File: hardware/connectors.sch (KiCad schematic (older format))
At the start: 16 parts

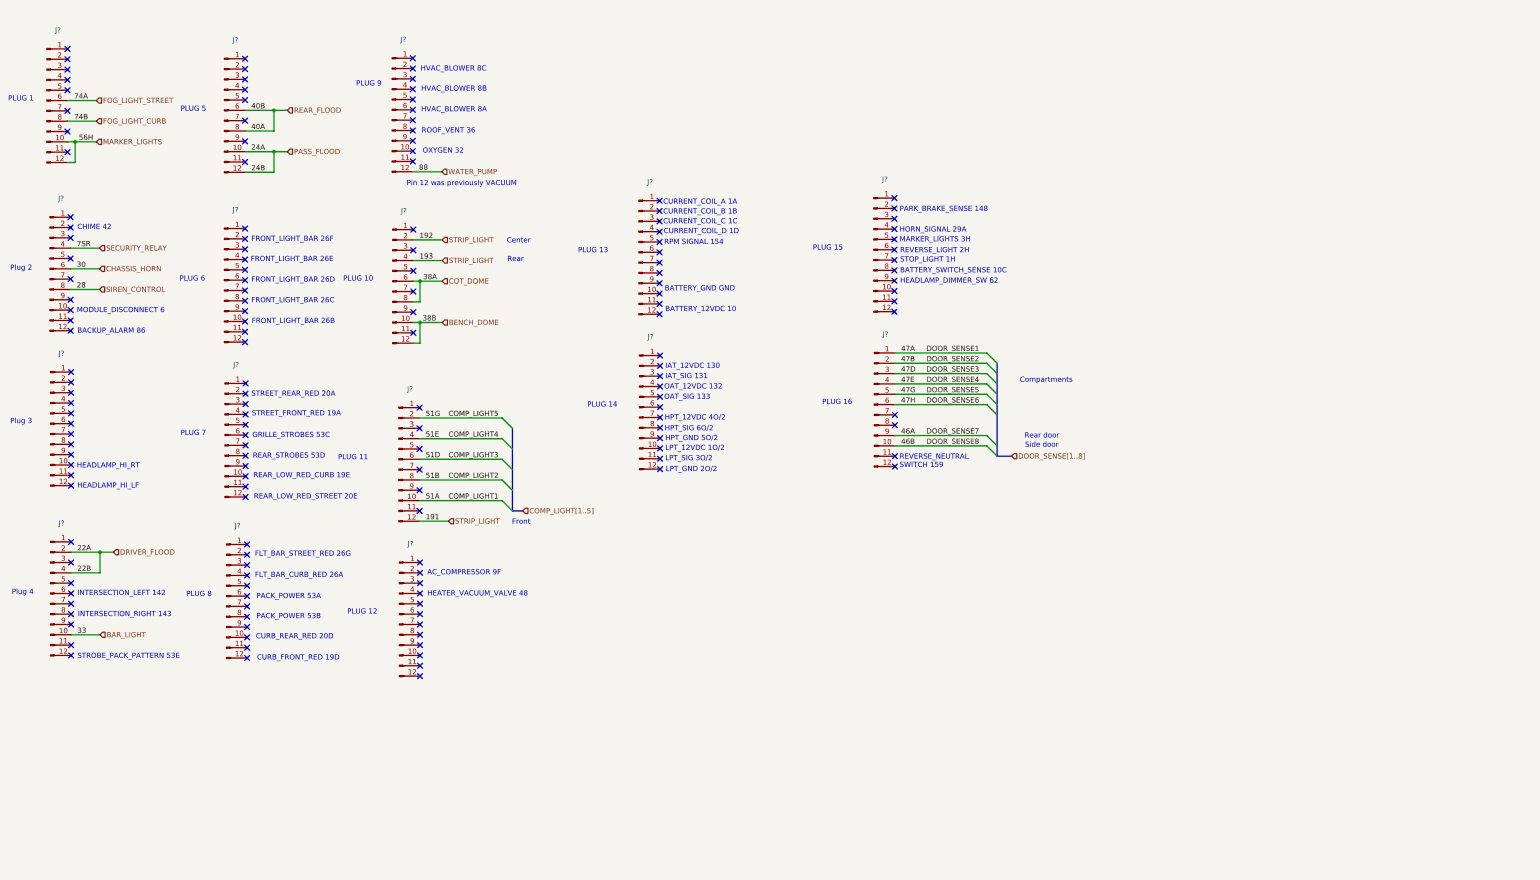
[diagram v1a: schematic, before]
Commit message: hardware: assign connectors corresponding references
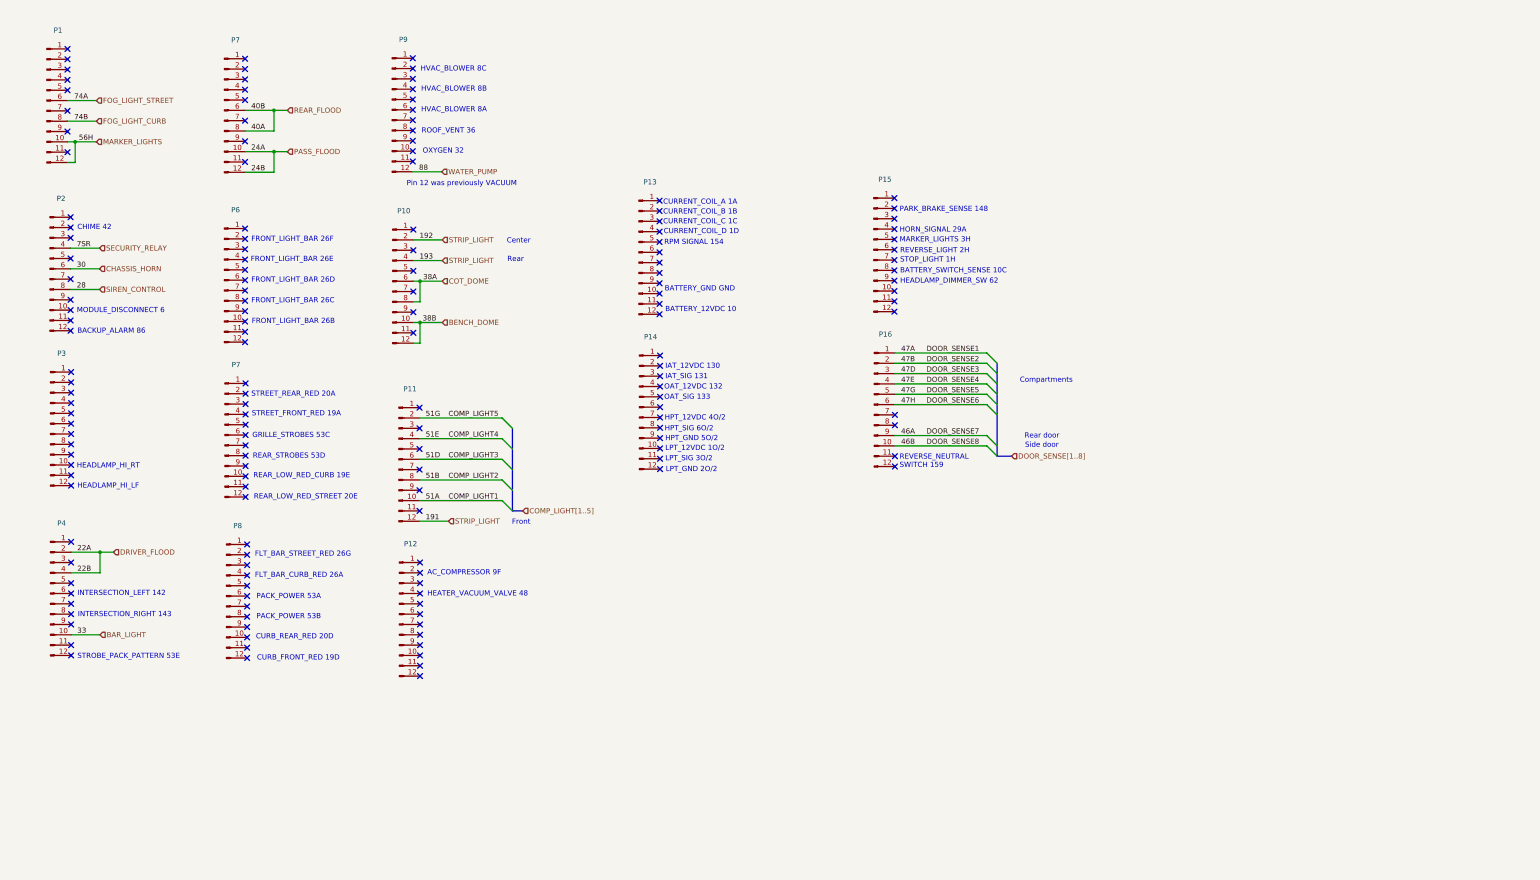
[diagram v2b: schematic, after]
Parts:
- gave numbers to parts that had none: 15
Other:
- note removed: "PLUG 1"
- note removed: "PLUG 10"
- note removed: "PLUG 11"
- note removed: "PLUG 12"
- note removed: "PLUG 13"
- note removed: "PLUG 14"
- note removed: "PLUG 15"
- note removed: "PLUG 16"
- note removed: "PLUG 5"
- note removed: "PLUG 6"
- note removed: "PLUG 7"
- note removed: "PLUG 8"
- note removed: "PLUG 9"
- note removed: "Plug 2"
- note removed: "Plug 3"
- note removed: "Plug 4"
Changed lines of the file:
@@
 P 1040 3290
 AR Path="/6060FD51" Ref="J?"  Part="1"
-AR Path="/605C149A/6060FD51" Ref="J?"  Part="1"
-F 0 "J?" H 1148 3971 50  0000 C CNN
+AR Path="/605C149A/6060FD51" Ref="P2"  Part="1"
+F 0 "P2" H 1148 3971 50  0000 C CNN
 F 1 "Conn_01x12_Male" H 1148 3880 50  0001 C CNN
 F 2 "Connector_Molex:Molex_KK-396_A-41791-0012_1x12_P3.96mm_Vertical" H 1040 3290 50  0001 C CNN
@@
 P 1045 4790
 AR Path="/60615EDC" Ref="J?"  Part="1"
-AR Path="/605C149A/60615EDC" Ref="J?"  Part="1"
-F 0 "J?" H 1153 5471 50  0000 C CNN
+AR Path="/605C149A/60615EDC" Ref="P3"  Part="1"
+F 0 "P3" H 1153 5471 50  0000 C CNN
 F 1 "Conn_01x12_Male" H 1153 5380 50  0001 C CNN
 F 2 "Connector_Molex:Molex_KK-396_A-41791-0012_1x12_P3.96mm_Vertical" H 1045 4790 50  0001 C CNN
@@
 P 1045 6435
 AR Path="/60615F08" Ref="J?"  Part="1"
-AR Path="/605C149A/60615F08" Ref="J?"  Part="1"
-F 0 "J?" H 1153 7116 50  0000 C CNN
+AR Path="/605C149A/60615F08" Ref="P4"  Part="1"
+F 0 "P4" H 1153 7116 50  0000 C CNN
 F 1 "Conn_01x12_Male" H 1153 7025 50  0001 C CNN
 F 2 "Connector_Molex:Molex_KK-396_A-41791-0012_1x12_P3.96mm_Vertical" H 1045 6435 50  0001 C CNN
@@
 P 2730 1755
 AR Path="/6062FF98" Ref="J?"  Part="1"
-AR Path="/605C149A/6062FF98" Ref="J?"  Part="1"
-F 0 "J?" H 2838 2436 50  0000 C CNN
+AR Path="/605C149A/6062FF98" Ref="P7"  Part="1"
+F 0 "P7" H 2838 2436 50  0000 C CNN
 F 1 "Conn_01x12_Male" H 2838 2345 50  0001 C CNN
 F 2 "Connector_Molex:Molex_KK-396_A-41791-0012_1x12_P3.96mm_Vertical" H 2730 1755 50  0001 C CNN
@@
 P 2730 3400
 AR Path="/6062FFC4" Ref="J?"  Part="1"
-AR Path="/605C149A/6062FFC4" Ref="J?"  Part="1"
-F 0 "J?" H 2838 4081 50  0000 C CNN
+AR Path="/605C149A/6062FFC4" Ref="P6"  Part="1"
+F 0 "P6" H 2838 4081 50  0000 C CNN
 F 1 "Conn_01x12_Male" H 2838 3990 50  0001 C CNN
 F 2 "Connector_Molex:Molex_KK-396_A-41791-0012_1x12_P3.96mm_Vertical" H 2730 3400 50  0001 C CNN
@@
 P 2735 4900
 AR Path="/6062FFF0" Ref="J?"  Part="1"
-AR Path="/605C149A/6062FFF0" Ref="J?"  Part="1"
-F 0 "J?" H 2843 5581 50  0000 C CNN
+AR Path="/605C149A/6062FFF0" Ref="P7"  Part="1"
+F 0 "P7" H 2843 5581 50  0000 C CNN
 F 1 "Conn_01x12_Male" H 2843 5490 50  0001 C CNN
 F 2 "Connector_Molex:Molex_KK-396_A-41791-0012_1x12_P3.96mm_Vertical" H 2735 4900 50  0001 C CNN
@@
 P 2750 6460
 AR Path="/6064FE96" Ref="J?"  Part="1"
-AR Path="/605C149A/6064FE96" Ref="J?"  Part="1"
-F 0 "J?" H 2858 7141 50  0000 C CNN
+AR Path="/605C149A/6064FE96" Ref="P8"  Part="1"
+F 0 "P8" H 2858 7141 50  0000 C CNN
 F 1 "Conn_01x12_Male" H 2858 7050 50  0001 C CNN
 F 2 "Connector_Molex:Molex_KK-396_A-41791-0012_1x12_P3.96mm_Vertical" H 2750 6460 50  0001 C CNN
@@
 P 4355 1750
 AR Path="/6064FEC2" Ref="J?"  Part="1"
-AR Path="/605C149A/6064FEC2" Ref="J?"  Part="1"
-F 0 "J?" H 4463 2431 50  0000 C CNN
+AR Path="/605C149A/6064FEC2" Ref="P9"  Part="1"
+F 0 "P9" H 4463 2431 50  0000 C CNN
 F 1 "Conn_01x12_Male" H 4463 2340 50  0001 C CNN
 F 2 "Connector_Molex:Molex_KK-396_A-41791-0012_1x12_P3.96mm_Vertical" H 4355 1750 50  0001 C CNN
@@
 P 4360 3410
 AR Path="/6064FEEE" Ref="J?"  Part="1"
-AR Path="/605C149A/6064FEEE" Ref="J?"  Part="1"
-F 0 "J?" H 4468 4091 50  0000 C CNN
+AR Path="/605C149A/6064FEEE" Ref="P10"  Part="1"
+F 0 "P10" H 4468 4091 50  0000 C CNN
 F 1 "Conn_01x12_Male" H 4468 4000 50  0001 C CNN
 F 2 "Connector_Molex:Molex_KK-396_A-41791-0012_1x12_P3.96mm_Vertical" H 4360 3410 50  0001 C CNN
@@
 P 4425 6635
 AR Path="/60662444" Ref="J?"  Part="1"
-AR Path="/605C149A/60662444" Ref="J?"  Part="1"
-F 0 "J?" H 4533 7316 50  0000 C CNN
+AR Path="/605C149A/60662444" Ref="P12"  Part="1"
+F 0 "P12" H 4533 7316 50  0000 C CNN
 F 1 "Conn_01x12_Male" H 4533 7225 50  0001 C CNN
 F 2 "Connector_Molex:Molex_KK-396_A-41791-0012_1x12_P3.96mm_Vertical" H 4425 6635 50  0001 C CNN
@@
 P 4420 5135
 AR Path="/60662418" Ref="J?"  Part="1"
-AR Path="/605C149A/60662418" Ref="J?"  Part="1"
-F 0 "J?" H 4528 5816 50  0000 C CNN
+AR Path="/605C149A/60662418" Ref="P11"  Part="1"
+F 0 "P11" H 4528 5816 50  0000 C CNN
 F 1 "Conn_01x12_Male" H 4528 5725 50  0001 C CNN
 F 2 "Connector_Molex:Molex_KK-396_A-41791-0012_1x12_P3.96mm_Vertical" H 4420 5135 50  0001 C CNN
@@
 	1    0    0    -1
 $EndComp
-Text Notes 635  1675 0    50   ~ 0
-PLUG 1
-Text Notes 655  3315 0    50   ~ 0
-Plug 2
-Text Notes 655  4800 0    50   ~ 0
-Plug 3
-Text Notes 670  6455 0    50   ~ 0
-Plug 4
-Text Notes 2305 1775 0    50   ~ 0
-PLUG 5
-Text Notes 2295 3420 0    50   ~ 0
-PLUG 6
-Text Notes 2305 4915 0    50   ~ 0
-PLUG 7
-Text Notes 2360 6475 0    50   ~ 0
-PLUG 8
-Text Notes 3920 6645 0    50   ~ 0
-PLUG 12
-Text Notes 3830 5150 0    50   ~ 0
-PLUG 11
-Text Notes 3880 3420 0    50   ~ 0
-PLUG 10
-Text Notes 4005 1530 0    50   ~ 0
-PLUG 9
 $Comp
 L Connector:Conn_01x12_Male J?
@@
 P 6750 4630
 AR Path="/606FB357" Ref="J?"  Part="1"
-AR Path="/605C149A/606FB357" Ref="J?"  Part="1"
-F 0 "J?" H 6858 5311 50  0000 C CNN
+AR Path="/605C149A/606FB357" Ref="P14"  Part="1"
+F 0 "P14" H 6858 5311 50  0000 C CNN
 F 1 "Conn_01x12_Male" H 6858 5220 50  0001 C CNN
 F 2 "Connector_Molex:Molex_KK-396_A-41791-0012_1x12_P3.96mm_Vertical" H 6750 4630 50  0001 C CNN
@@
 P 6745 3130
 AR Path="/606FB35D" Ref="J?"  Part="1"
-AR Path="/605C149A/606FB35D" Ref="J?"  Part="1"
-F 0 "J?" H 6853 3811 50  0000 C CNN
+AR Path="/605C149A/606FB35D" Ref="P13"  Part="1"
+F 0 "P13" H 6853 3811 50  0000 C CNN
 F 1 "Conn_01x12_Male" H 6853 3720 50  0001 C CNN
 F 2 "Connector_Molex:Molex_KK-396_A-41791-0012_1x12_P3.96mm_Vertical" H 6745 3130 50  0001 C CNN
@@
 	1    0    0    -1
 $EndComp
-Text Notes 6245 4640 0    50   ~ 0
-PLUG 14
-Text Notes 6155 3145 0    50   ~ 0
-PLUG 13
 $Comp
 L Connector:Conn_01x12_Male J?
@@
 P 9025 4605
 AR Path="/606FDCF1" Ref="J?"  Part="1"
-AR Path="/605C149A/606FDCF1" Ref="J?"  Part="1"
-F 0 "J?" H 9133 5286 50  0000 C CNN
+AR Path="/605C149A/606FDCF1" Ref="P16"  Part="1"
+F 0 "P16" H 9133 5286 50  0000 C CNN
 F 1 "Conn_01x12_Male" H 9133 5195 50  0001 C CNN
 F 2 "Connector_Molex:Molex_KK-396_A-41791-0012_1x12_P3.96mm_Vertical" H 9025 4605 50  0001 C CNN
@@
 P 9020 3105
 AR Path="/606FDCF7" Ref="J?"  Part="1"
-AR Path="/605C149A/606FDCF7" Ref="J?"  Part="1"
-F 0 "J?" H 9128 3786 50  0000 C CNN
+AR Path="/605C149A/606FDCF7" Ref="P15"  Part="1"
+F 0 "P15" H 9128 3786 50  0000 C CNN
 F 1 "Conn_01x12_Male" H 9128 3695 50  0001 C CNN
 F 2 "Connector_Molex:Molex_KK-396_A-41791-0012_1x12_P3.96mm_Vertical" H 9020 3105 50  0001 C CNN
@@
 	1    0    0    -1
 $EndComp
-Text Notes 8520 4615 0    50   ~ 0
-PLUG 16
-Text Notes 8430 3120 0    50   ~ 0
-PLUG 15
 $Comp
 L Connector:Conn_01x12_Male J?
@@
 P 1010 1660
 AR Path="/607423B0" Ref="J?"  Part="1"
-AR Path="/605C149A/607423B0" Ref="J?"  Part="1"
-F 0 "J?" H 1118 2341 50  0000 C CNN
+AR Path="/605C149A/607423B0" Ref="P1"  Part="1"
+F 0 "P1" H 1118 2341 50  0000 C CNN
 F 1 "Conn_01x12_Male" H 1118 2250 50  0001 C CNN
 F 2 "Connector_Molex:Molex_KK-396_A-41791-0012_1x12_P3.96mm_Vertical" H 1010 1660 50  0001 C CNN

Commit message: hardware: use busses for plug connections
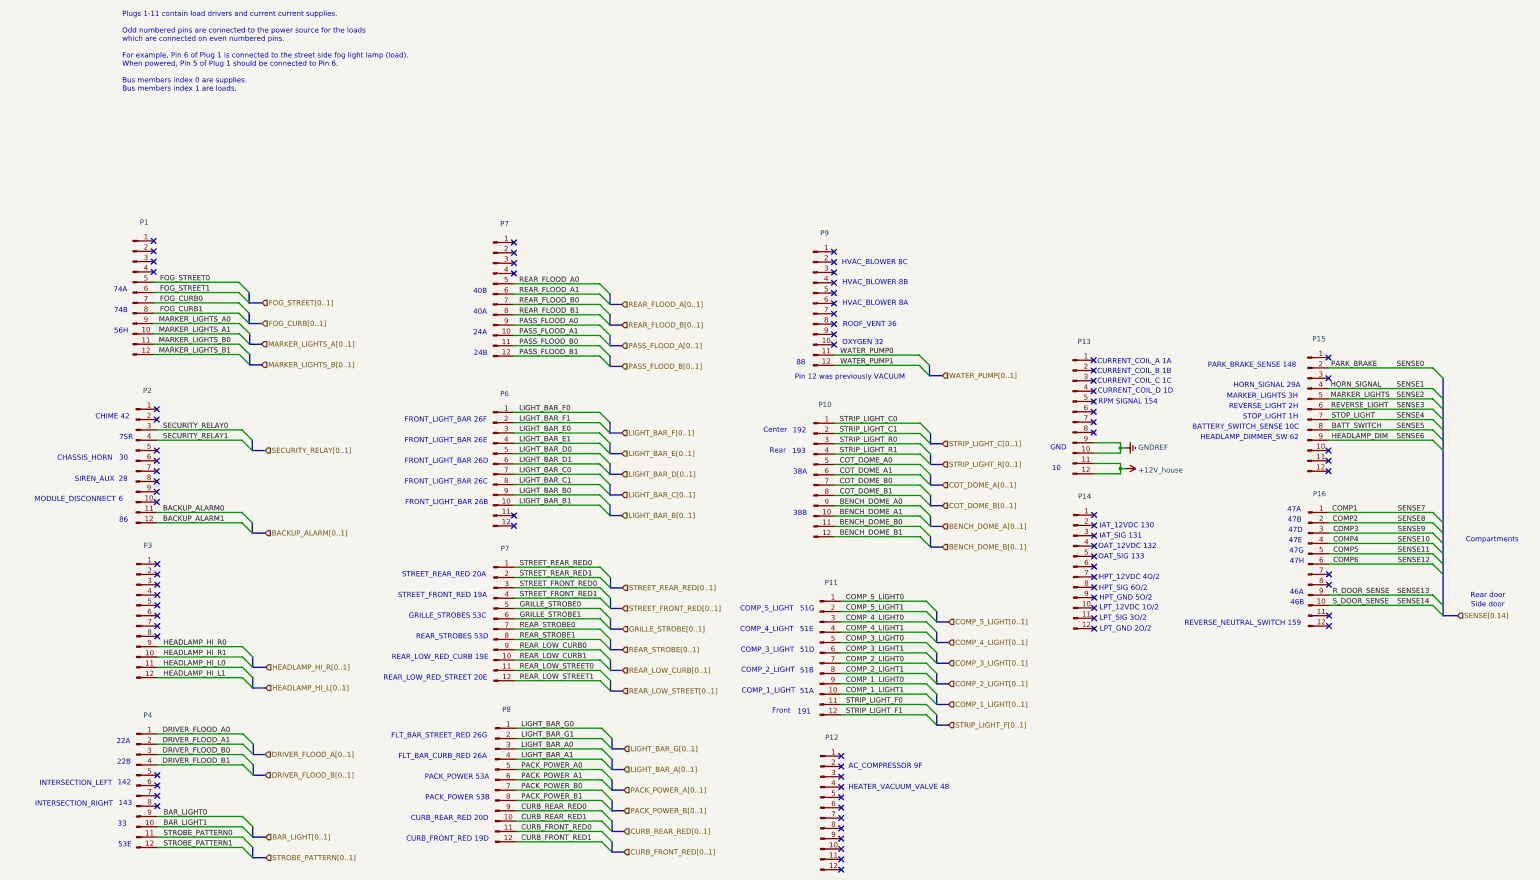
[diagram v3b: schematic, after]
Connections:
- net MARKER_LIGHTS: now also P15.5 (Pin_5); no longer P1.10 (Pin_10), P1.12 (Pin_12)
- net BACKUP_ALARM0: now reaches P2.11 (Pin_11)
- net BACKUP_ALARM1: now reaches P2.12 (Pin_12)
- net SECURITY_RELAY0: now reaches P2.3 (Pin_3)
- net HEADLAMP_HI_R1: now reaches P3.10 (Pin_10)
- net HEADLAMP_HI_L0: now reaches P3.11 (Pin_11)
- net HEADLAMP_HI_L1: now reaches P3.12 (Pin_12)
- net HEADLAMP_HI_R0: now reaches P3.9 (Pin_9)
- net DRIVER_FLOOD_A0: now reaches P4.1 (Pin_1)
- net STROBE_PATTERN0: now reaches P4.11 (Pin_11)
- net STROBE_PATTERN1: now reaches P4.12 (Pin_12)
- net DRIVER_FLOOD_B0: now reaches P4.3 (Pin_3)
- net BAR_LIGHT0: now reaches P4.9 (Pin_9)
- net PASS_FLOOD_B0: now reaches P7.11 (Pin_11)
- net REAR_FLOOD_A0: now reaches P7.5 (Pin_5)
- net REAR_FLOOD_B0: now reaches P7.7 (Pin_7)
- net PASS_FLOOD_A0: now reaches P7.9 (Pin_9)
- net LIGHT_BAR_F0: now reaches P6.1 (Pin_1)
- net LIGHT_BAR_B1: now reaches P6.10 (Pin_10)
- net LIGHT_BAR_F1: now reaches P6.2 (Pin_2)
- net LIGHT_BAR_E0: now reaches P6.3 (Pin_3)
- net LIGHT_BAR_E1: now reaches P6.4 (Pin_4)
- net LIGHT_BAR_D0: now reaches P6.5 (Pin_5)
- net LIGHT_BAR_D1: now reaches P6.6 (Pin_6)
- net LIGHT_BAR_C0: now reaches P6.7 (Pin_7)
- net LIGHT_BAR_C1: now reaches P6.8 (Pin_8)
- net LIGHT_BAR_B0: now reaches P6.9 (Pin_9)
- net STREET_REAR_RED0: now reaches P7.1 (Pin_1)
- net REAR_LOW_CURB1: now reaches P7.10 (Pin_10)
- net REAR_LOW_STREET0: now reaches P7.11 (Pin_11)
- net REAR_LOW_STREET1: now reaches P7.12 (Pin_12)
- net STREET_REAR_RED1: now reaches P7.2 (Pin_2)
- net STREET_FRONT_RED0: now reaches P7.3 (Pin_3)
- net STREET_FRONT_RED1: now reaches P7.4 (Pin_4)
- net GRILLE_STROBE0: now reaches P7.5 (Pin_5)
- net GRILLE_STROBE1: now reaches P7.6 (Pin_6)
- net REAR_STROBE0: now reaches P7.7 (Pin_7)
- net REAR_STROBE1: now reaches P7.8 (Pin_8)
- net REAR_LOW_CURB0: now reaches P7.9 (Pin_9)
- net LIGHT_BAR_G0: now reaches P8.1 (Pin_1)
- net CURB_REAR_RED1: now reaches P8.10 (Pin_10)
- net CURB_FRONT_RED0: now reaches P8.11 (Pin_11)
- net CURB_FRONT_RED1: now reaches P8.12 (Pin_12)
- net LIGHT_BAR_G1: now reaches P8.2 (Pin_2)
- net LIGHT_BAR_A0: now reaches P8.3 (Pin_3)
- net LIGHT_BAR_A1: now reaches P8.4 (Pin_4)
- net PACK_POWER_A0: now reaches P8.5 (Pin_5)
- net PACK_POWER_A1: now reaches P8.6 (Pin_6)
- net PACK_POWER_B0: now reaches P8.7 (Pin_7)
- net PACK_POWER_B1: now reaches P8.8 (Pin_8)
- net CURB_REAR_RED0: now reaches P8.9 (Pin_9)
- net WATER_PUMP0: now reaches P9.11 (Pin_11)
- net STRIP_LIGHT_C0: now reaches P10.1 (Pin_1)
- net BENCH_DOME_B0: now reaches P10.11 (Pin_11)
- net STRIP_LIGHT_R0: now reaches P10.3 (Pin_3)
- net COT_DOME_A0: now reaches P10.5 (Pin_5)
- net COT_DOME_B0: now reaches P10.7 (Pin_7)
- net BENCH_DOME_A0: now reaches P10.9 (Pin_9)
- net COMP_5_LIGHT0: now reaches P11.1 (Pin_1)
- net STRIP_LIGHT_F0: now reaches P11.11 (Pin_11)
- net COMP_4_LIGHT0: now reaches P11.3 (Pin_3)
- net COMP_3_LIGHT0: now reaches P11.5 (Pin_5)
- net COMP_2_LIGHT0: now reaches P11.7 (Pin_7)
- net COMP_1_LIGHT0: now reaches P11.9 (Pin_9)
- net GNDREF: now reaches P13.10 (Pin_10)
- net GNDREF: now also P13.9 (Pin_9)
- net +12V: now reaches P13.11 (Pin_11)
- net +12V: now also P13.12 (Pin_12)
- net PARK_BRAKE: now reaches P15.2 (Pin_2)
- net HORN_SIGNAL: now reaches P15.4 (Pin_4)
- net REVERSE_LIGHT: now reaches P15.6 (Pin_6)
- net SENSE4: now reaches P15.7 (Pin_7)
- net BATT_SWITCH: now reaches P15.8 (Pin_8)
- net HEADLAMP_DIM: now reaches P15.9 (Pin_9)
- net MARKER_LIGHTS_B0: now reaches P1.11 (Pin_11)
- net FOG_STREET0: now reaches P1.5 (Pin_5)
- net FOG_CURB0: now reaches P1.7 (Pin_7)
- net MARKER_LIGHTS_A0: now reaches P1.9 (Pin_9)
- net 46A renamed R_DOOR_SENSE
- net 46B renamed SENSE14
- net 47A renamed COMP1
- net 47B renamed COMP2
- net 47D renamed COMP3
- net 47E renamed COMP4
- net 47G renamed COMP5
- net 47H renamed COMP6
- net 51A renamed COMP_1_LIGHT1
- net 51B renamed COMP_2_LIGHT1
- net 51D renamed COMP_3_LIGHT1
- net 51E renamed COMP_4_LIGHT1
- net 51G renamed COMP_5_LIGHT1
- net BAR_LIGHT renamed BAR_LIGHT1
- net BENCH_DOME renamed BENCH_DOME_A1
- net BENCH_DOME_A1: no longer P10.12 (Pin_12)
- net CHASSIS_HORN: no longer names the net of P2.6 (Pin_6)
- net COT_DOME renamed COT_DOME_A1
- net COT_DOME_A1: no longer P10.8 (Pin_8)
- net DRIVER_FLOOD renamed DRIVER_FLOOD_A1
- net DRIVER_FLOOD_A1: no longer P4.4 (Pin_4)
- net FOG_LIGHT_CURB renamed FOG_CURB1
- net FOG_LIGHT_STREET renamed FOG_STREET1
- net PASS_FLOOD renamed PASS_FLOOD_A1
- net PASS_FLOOD_A1: no longer P7.12 (Pin_12)
- net REAR_FLOOD renamed REAR_FLOOD_A1
- net REAR_FLOOD_A1: no longer P7.8 (Pin_8)
- net SECURITY_RELAY renamed SECURITY_RELAY1
- net SIREN_CONTROL: no longer names the net of P2.8 (Pin_8)
- removed net STRIP_LIGHT: P10.2 (Pin_2), P10.4 (Pin_4), P11.12 (Pin_12)
- net WATER_PUMP renamed WATER_PUMP1
- new net BENCH_DOME_B1: P10.12 (Pin_12)
- new net COT_DOME_B1: P10.8 (Pin_8)
- new net DRIVER_FLOOD_B1: P4.4 (Pin_4)
- new net MARKER_LIGHTS_A1: P1.10 (Pin_10)
- new net MARKER_LIGHTS_B1: P1.12 (Pin_12)
- new net PASS_FLOOD_B1: P7.12 (Pin_12)
- new net REAR_FLOOD_B1: P7.8 (Pin_8)
- new net STRIP_LIGHT_C1: P10.2 (Pin_2)
- new net STRIP_LIGHT_F1: P11.12 (Pin_12)
- new net STRIP_LIGHT_R1: P10.4 (Pin_4)
- no-connect marks 157 -> 81
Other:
- note added: "10"
- note added: "142"
- note added: "143"
- note added: "191"
- note added: "192"
- note added: "193"
- note added: "22A"
- note added: "22B"
- note added: "24A"
- note added: "24B"
- note added: "28"
- note added: "30"
- note added: "33"
- note added: "38A"
- note added: "38B"
- note added: "40A"
- note added: "40B"
- note added: "46A"
- note added: "46B"
- note added: "47A"
- note added: "47B"
- note added: "47D"
- note added: "47E"
- note added: "47G"
- note added: "47H"
- note added: "51A"
- note added: "51B"
- note added: "51D"
- note added: "51E"
- note added: "51G"
- note added: "53E"
- note added: "56H"
- note added: "6"
- note added: "74A"
- note added: "74B"
- note added: "7SR"
- note added: "86"
- note added: "88"
- note added: "CHASSIS_HORN"
- note added: "COMP_1_LIGHT"
- note added: "COMP_2_LIGHT"
- note added: "COMP_3_LIGHT"
- note added: "COMP_4_LIGHT"
- note added: "COMP_5_LIGHT"
- note added: "GND"
- note added: "INTERSECTION_LEFT"
- note added: "INTERSECTION_RIGHT"
- note added: "MODULE_DISCONNECT"
- note added: "Plugs 1-11 contain load drivers and current current supplies.\n\nOdd numbered pins are connected to the power source for the loads\nwhich are connected on even numbered pins.\n\nFor example, Pin 6 of Plug 1 is connected to the street side fog light lamp (load). \nWhen powered, Pin 5 of Plug 1 should be connected to Pin 6.\n\nBus members index 0 are supplies.\nBus members index 1 are loads."
- note added: "REVERSE_NEUTRAL_SWITCH 159"
- note added: "SIREN_AUX"
- note removed: "BACKUP_ALARM 86"
- note removed: "BATTERY_12VDC 10"
- note removed: "BATTERY_GND GND"
- note removed: "HEADLAMP_HI_LF"
- note removed: "HEADLAMP_HI_RT"
- note removed: "INTERSECTION_LEFT 142"
- note removed: "INTERSECTION_RIGHT 143"
- note removed: "MODULE_DISCONNECT 6"
- note removed: "REVERSE_NEUTRAL\nSWITCH 159"
- note removed: "STROBE_PACK_PATTERN 53E"
- moved on the sheet: P1, P10, P11, P12, P13, P14, P15, P16, P2, P3, P4, P6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
